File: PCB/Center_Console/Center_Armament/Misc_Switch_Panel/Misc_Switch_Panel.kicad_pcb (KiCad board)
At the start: 2 copper layers, 1 part

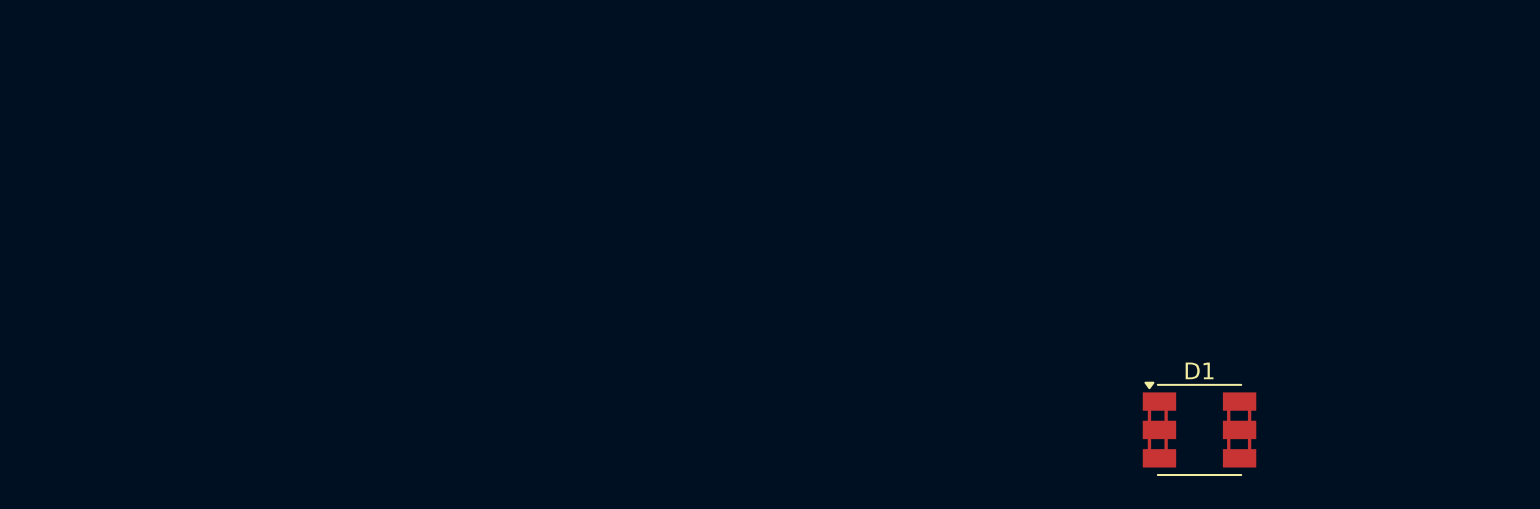
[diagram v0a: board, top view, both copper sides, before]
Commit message: Misc Switch Panel schematic WIP + gitignore cleanup
- Misc_Switch_Panel: schematic and PCB in-progress (MCP23017, 8-pin JST-XH harness)
- .gitignore: exclude KiCad Fabrication Toolkit outputs (production/, fabrication-toolkit-options.json) and .claude/worktrees/
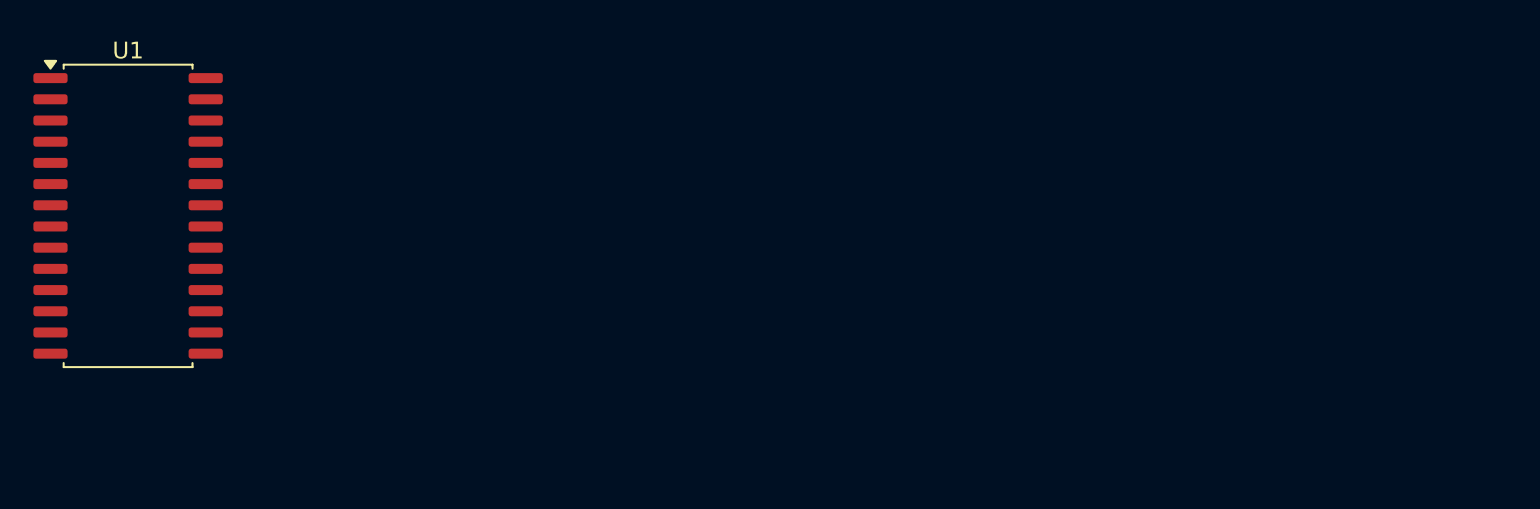
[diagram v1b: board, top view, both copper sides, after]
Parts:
- removed D1: LED_5050_Red, OpenSkyhawk:LED_5050_Red
- added U1: MCP23017x-x-SO, Package_SO:SOIC-28W_7.5x17.9mm_P1.27mm, F.Cu at (75.8, 69.7)

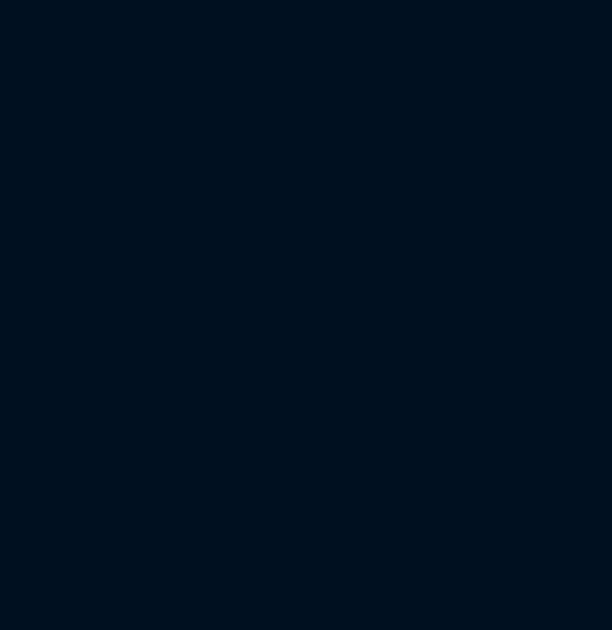
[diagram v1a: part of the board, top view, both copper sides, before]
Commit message: Scaffold AWRS_Panel and Armament_MCU KiCad projects
- AWRS_Panel: breakout board scaffold (sym-lib-table, fp-lib-table,
  jlcpcb-standard.kicad_dru, .kicad_pro, .kicad_sch)
- Armament_MCU: MCU board scaffold (same set of files)
- Add controller stub docs: AWRS_Panel.md and Armament_Panel.md
- Update Center_Armament.md harness section: J1→AWRS_Panel and
  J2→Misc_Switch_Panel documented as two distinct connectors with
  full pinouts; J2_LED Mini-Fit Jr added
- Misc_Switch_Panel: KiCad reformatted files on project open
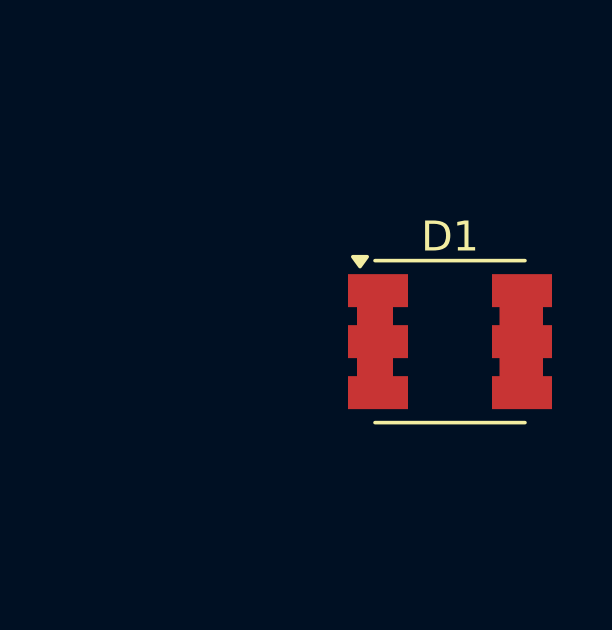
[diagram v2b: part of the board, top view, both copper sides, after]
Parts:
- added D1: LED_5050_Red, OpenSkyhawk:LED_5050_Red, F.Cu at (155.0, 70.0)
